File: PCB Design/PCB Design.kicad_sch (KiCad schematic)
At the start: 1 part, among them U1 ESP32-WROOM-32

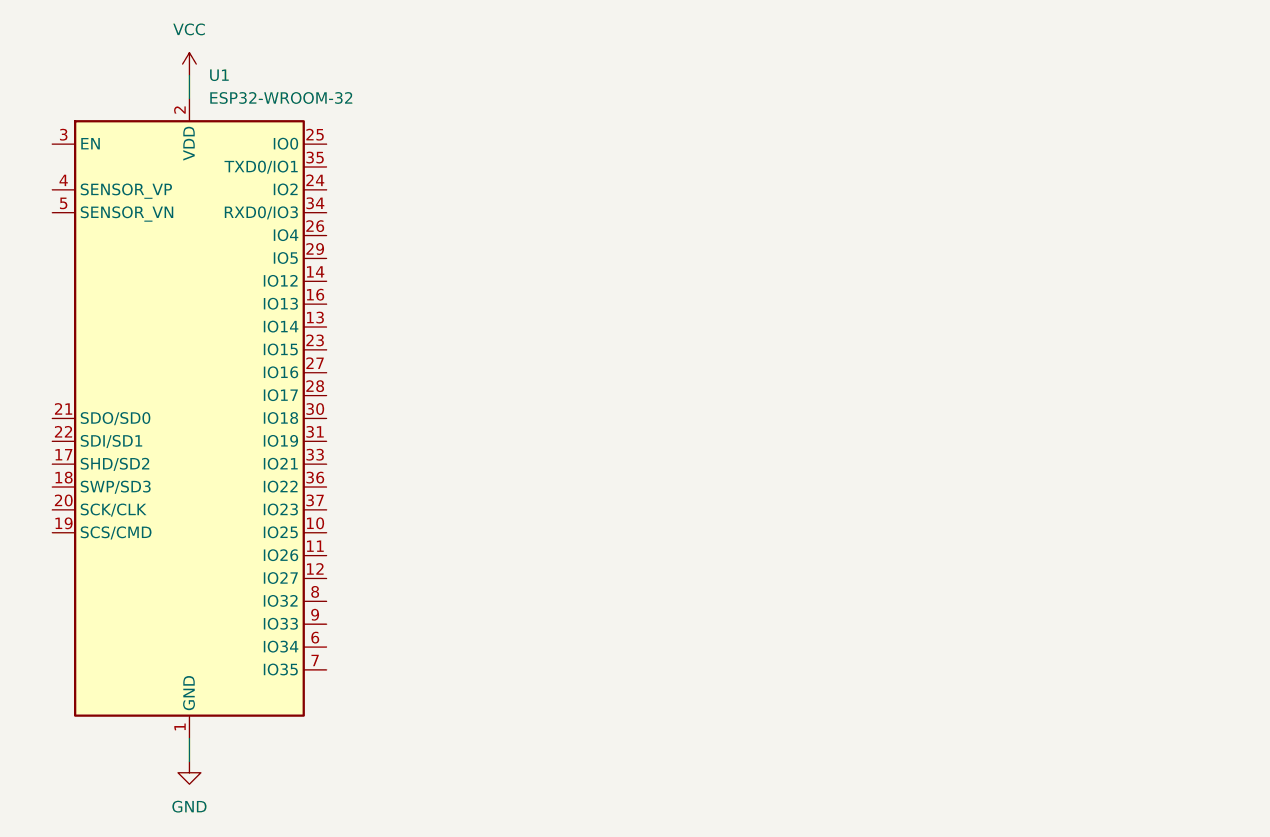
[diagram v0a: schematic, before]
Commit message: Relay PCB design finished next is the connection for the sensors and connecting the relay to the microcontroller.
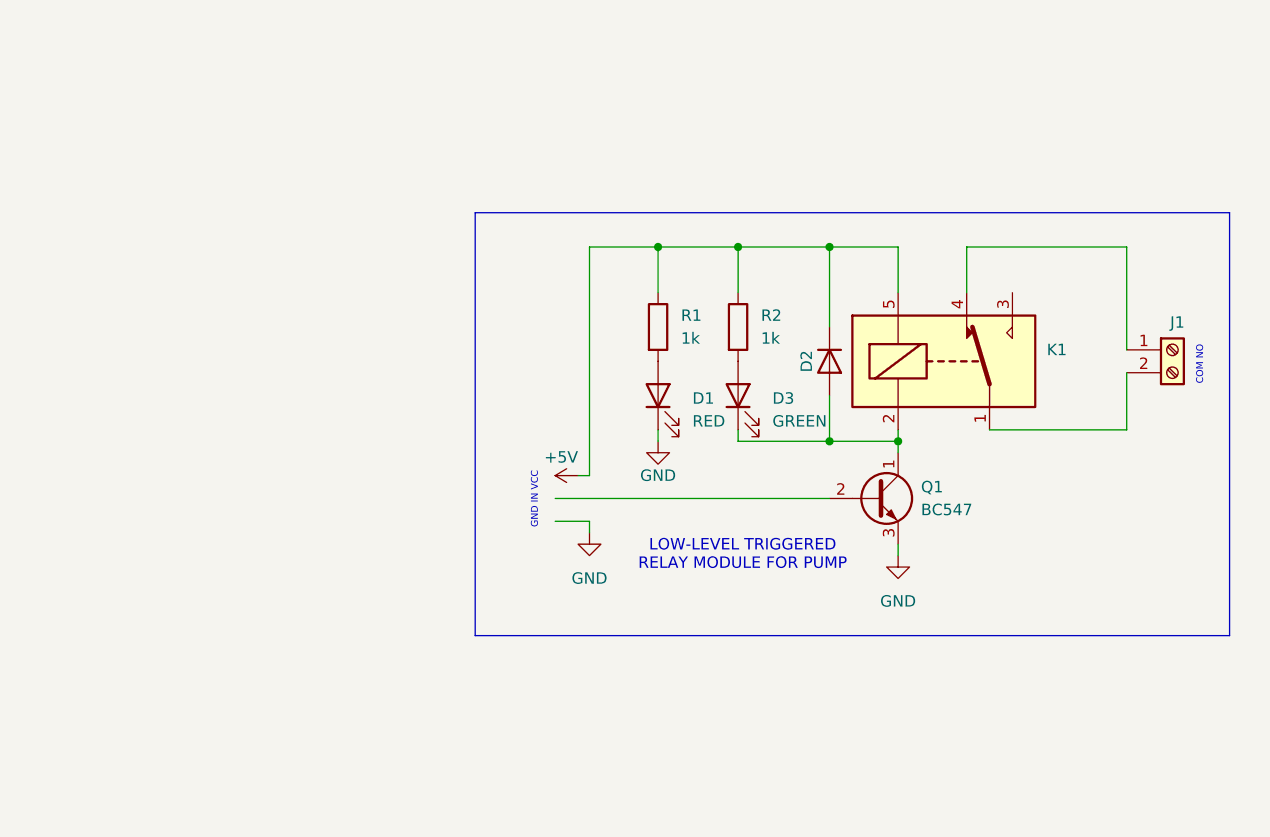
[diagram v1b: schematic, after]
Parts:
- removed U1: ESP32-WROOM-32, RF_Module:ESP32-WROOM-32, symbol RF_Module:ESP32-WROOM-32
- added D1: RED, LED_SMD:LED_01005_0402Metric, symbol Device:LED
- added D2: 1N4007, Diode_THT:D_DO-41_SOD81_P10.16mm_Horizontal, symbol Diode:1N4007
- added D3: GREEN, LED_SMD:LED_01005_0402Metric, symbol Device:LED
- added J1: Screw_Terminal_01x02, TerminalBlock:TerminalBlock_MaiXu_MX126-5.0-02P_1x02_P5.00mm, symbol Connector:Screw_Terminal_01x02
- added K1: SANYOU_SRD_Form_C, Relay_THT:Relay_SPDT_SANYOU_SRD_Series_Form_C, symbol Relay:SANYOU_SRD_Form_C
- added Q1: BC547, Package_TO_SOT_THT:TO-92_Inline, symbol Transistor_BJT:BC547
- added R1, R2: 1k, Resistor_SMD:R_01005_0402Metric, symbol Device:R
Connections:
- net GND: now also D1.1 (K), Q1.3 (E)
- new net: J1.2 (Pin_2), K1.1
- new net: D2.2 (A), D3.1 (K), K1.2, Q1.1 (C)
- new net: J1.1 (Pin_1), K1.4
- new net: D3.2 (A), R2.2
- new net: D1.2 (A), R1.2
- new net +5V: D2.1 (K), K1.5, R1.1, R2.1
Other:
- note added: "COM NO"
- note added: "GND IN VCC"
- note added: "LOW-LEVEL TRIGGERED RELAY MODULE FOR PUMP"

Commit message: Finished the first version of the PCB design. Added the footprint library table and removed the lock file.
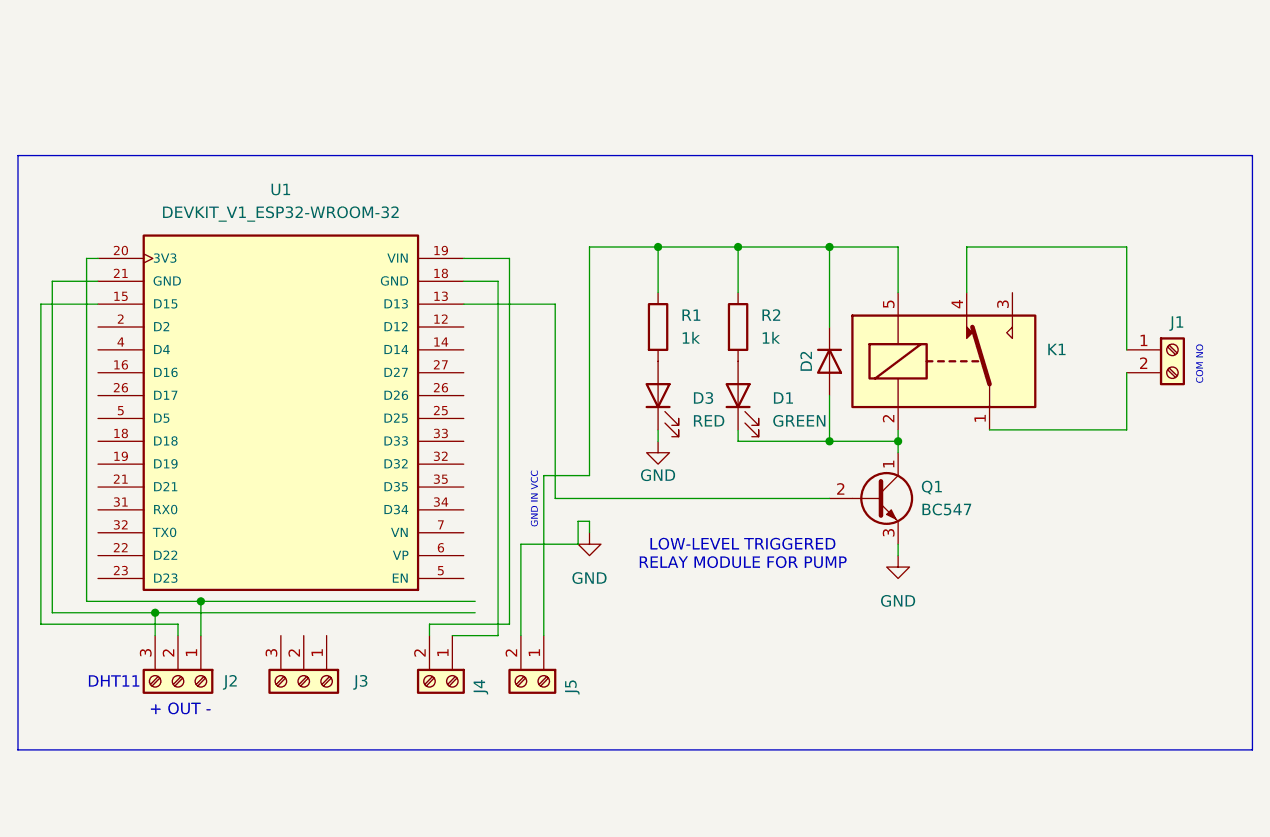
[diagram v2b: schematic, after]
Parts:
- added J2, J3: Screw_Terminal_01x03, TerminalBlock_Phoenix:TerminalBlock_Phoenix_MKDS-1,5-3-5.08_1x03_P5.08mm_Horizontal, symbol Connector:Screw_Terminal_01x03
- added J4, J5: Screw_Terminal_01x02, TerminalBlock_Phoenix:TerminalBlock_Phoenix_MKDS-1,5-2_1x02_P5.00mm_Horizontal, symbol Connector:Screw_Terminal_01x02
- added U1: DEVKIT_V1_ESP32-WROOM-32, DEVKIT_V1_ESP32-WROOM-32:MODULE_DEVKIT_V1_ESP32-WROOM-32, symbol DEVKIT_V1_ESP32-WROOM-32:DEVKIT_V1_ESP32-WROOM-32
- D1: renamed from D3; footprint LED_SMD:LED_01005_0402Metric -> LED_THT:LED_D5.0mm
- D3: renamed from D1; footprint LED_SMD:LED_01005_0402Metric -> LED_THT:LED_D5.0mm
- J1: footprint TerminalBlock:TerminalBlock_MaiXu_MX126-5.0-02P_1x02_P5.00mm -> TerminalBlock_Phoenix:TerminalBlock_Phoenix_MKDS-1,5-2_1x02_P5.00mm_Horizontal
- R1, R2: footprint Resistor_SMD:R_01005_0402Metric -> Resistor_THT:R_Axial_DIN0207_L6.3mm_D2.5mm_P7.62mm_Horizontal
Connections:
- net GND: now also J5.2 (Pin_2)
- net at Q1.2 (B): now also U1.13 (D13)
- net +5V: no longer names the net of D2.1 (K), K1.5, R1.1, R2.1
- net +5V: now also J5.1 (Pin_1)
- new net: J2.2 (Pin_2), U1.15 (D15)
- new net: J4.1 (Pin_1), U1.18 (D18)
- new net: J4.2 (Pin_2), U1.19 (D19)
- new net: J2.1 (Pin_1), U1.20 (3V3)
- new net: J2.3 (Pin_3), U1.21 (GND)
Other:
- note added: "+ OUT -"
- note added: "DHT11"

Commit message: Test
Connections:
- net at U1.12 (D12): now also J3.3 (Pin_3)
- net at U1.18 (D18): now also J4.1 (Pin_1)
- net at U1.19 (D19): now also J4.2 (Pin_2)
- net at J2.1 (Pin_1), U1.20 (3V3): now also J3.2 (Pin_2)
- net at U1.21 (GND): now also J2.3 (Pin_3), J3.1 (Pin_1)
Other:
- note added: "DATA VCC GND"
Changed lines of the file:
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@@
+		)
+	)
+	(text "DATA VCC GND "
+		(exclude_from_sim no)
+		(at 164.084 108.712 0)
+		(effects
+			(font
+				(size 0.762 0.762)
+			)
 		)
 	)
@@
 	(wire
 		(pts
+			(xy 158.75 100.33) (xy 161.29 100.33)
+		)
+		(stroke
+			(width 0)
+			(type default)
+		)
+	)
+	(wire
+		(pts
 			(xy 237.49 57.15) (xy 255.27 57.15)
 		)
@@
 	(wire
 		(pts
-			(xy 147.32 97.79) (xy 182.88 97.79)
+			(xy 147.32 97.79) (xy 166.37 97.79)
 		)
 		(stroke
@@
 	(wire
 		(pts
-			(xy 152.4 96.52) (xy 182.88 96.52)
+			(xy 184.15 66.04) (xy 184.15 110.49)
+		)
+		(stroke
+			(width 0)
+			(type default)
+		)
+	)
+	(wire
+		(pts
+			(xy 152.4 96.52) (xy 163.83 96.52)
 		)
 		(stroke
@@
 	(wire
 		(pts
+			(xy 163.83 96.52) (xy 163.83 100.33)
+		)
+		(stroke
+			(width 0)
+			(type default)
+		)
+	)
+	(wire
+		(pts
 			(xy 135.89 60.96) (xy 135.89 97.79)
 		)
@@
 	(wire
 		(pts
+			(xy 166.37 97.79) (xy 166.37 100.33)
+		)
+		(stroke
+			(width 0)
+			(type default)
+		)
+	)
+	(wire
+		(pts
 			(xy 195.58 87.63) (xy 195.58 88.9)
 		)
@@
 	(wire
 		(pts
+			(xy 184.15 110.49) (xy 158.75 110.49)
+		)
+		(stroke
+			(width 0)
+			(type default)
+		)
+	)
+	(wire
+		(pts
 			(xy 135.89 97.79) (xy 147.32 97.79)
 		)
@@
 	(wire
 		(pts
+			(xy 181.61 66.04) (xy 184.15 66.04)
+		)
+		(stroke
+			(width 0)
+			(type default)
+		)
+	)
+	(wire
+		(pts
 			(xy 222.25 78.74) (xy 229.87 78.74)
 		)
@@
 		)
 		(stroke
+			(width 0)
+			(type default)
+		)
+	)
+	(wire
+		(pts
+			(xy 158.75 110.49) (xy 158.75 100.33)
+		)
+		(stroke
